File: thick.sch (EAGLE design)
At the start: 25 parts, among them J1 43045-0400, Q1 SI2319DDS-T1-GE3, U1 ATTINY85-20SU

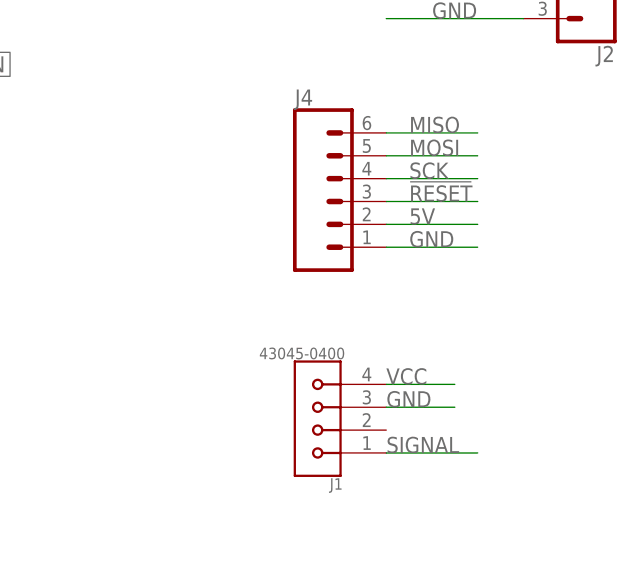
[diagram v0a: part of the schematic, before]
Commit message: Fixing
- sizes
- FPC connector
- Molex connector
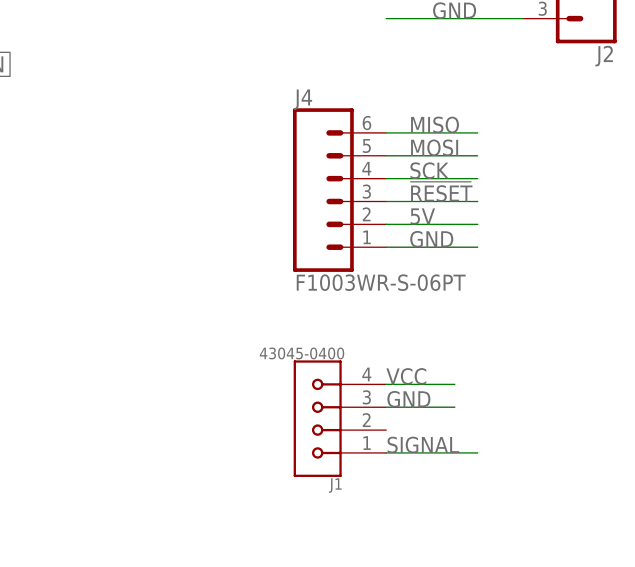
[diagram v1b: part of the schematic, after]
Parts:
- J4: value (none) -> F1003WR-S-06PT; device SparkFun-Connectors:CONN_06SMD-1MM -> FloManEagle:F1003WR-S-06PT
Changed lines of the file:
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@@
 <part name="GND6" library="SparkFun-PowerSymbols" library_urn="urn:adsk.eagle:library:530" deviceset="GND" device=""/>
 <part name="J2" library="SparkFun-Connectors" library_urn="urn:adsk.eagle:library:513" deviceset="CONN_03" device="LONGPADS" package3d_urn="urn:adsk.eagle:package:38068/1"/>
-<part name="J4" library="SparkFun-Connectors" library_urn="urn:adsk.eagle:library:513" deviceset="CONN_06" device="SMD-1MM" package3d_urn="urn:adsk.eagle:package:38023/1"/>
+<part name="J4" library="FloManEagle" deviceset="F1003WR-S-06PT" device=""/>
 <part name="C5" library="resistor" library_urn="urn:adsk.eagle:library:348" deviceset="C-EU" device="C0603" package3d_urn="urn:adsk.eagle:package:23616/2" value="0.1uF"/>
 <part name="C6" library="resistor" library_urn="urn:adsk.eagle:library:348" deviceset="C-EU" device="C1206" package3d_urn="urn:adsk.eagle:package:23618/2" value="10uF"/>

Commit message: Javított végleges
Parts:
- added T1: (no value), transistor:MUN2213T1-NPN_DRIVER-SC59-BEC
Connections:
- removed net !IGN_EN: C5.1, Q1.G, R3.1, U1.PB3
- new net IGN_EN: C5.1, T1.B, U1.PB3
- new net N$1: Q1.G, R3.1, T1.C
- net 5V: no longer R3.2
- net GND: now also T1.E
- net IGNITION: now also Q1.D; no longer Q1.S
- net VDD: now also Q1.S, R3.2; no longer Q1.D
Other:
- moved on the sheet: C2, C5, Q1, R3, R4
